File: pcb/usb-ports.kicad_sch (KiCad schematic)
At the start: 10 parts, among them J6 USB4105-GF-A, J7 USB4105-GF-A, U2 USBLC6-2P6, U3 USBLC6-2P6

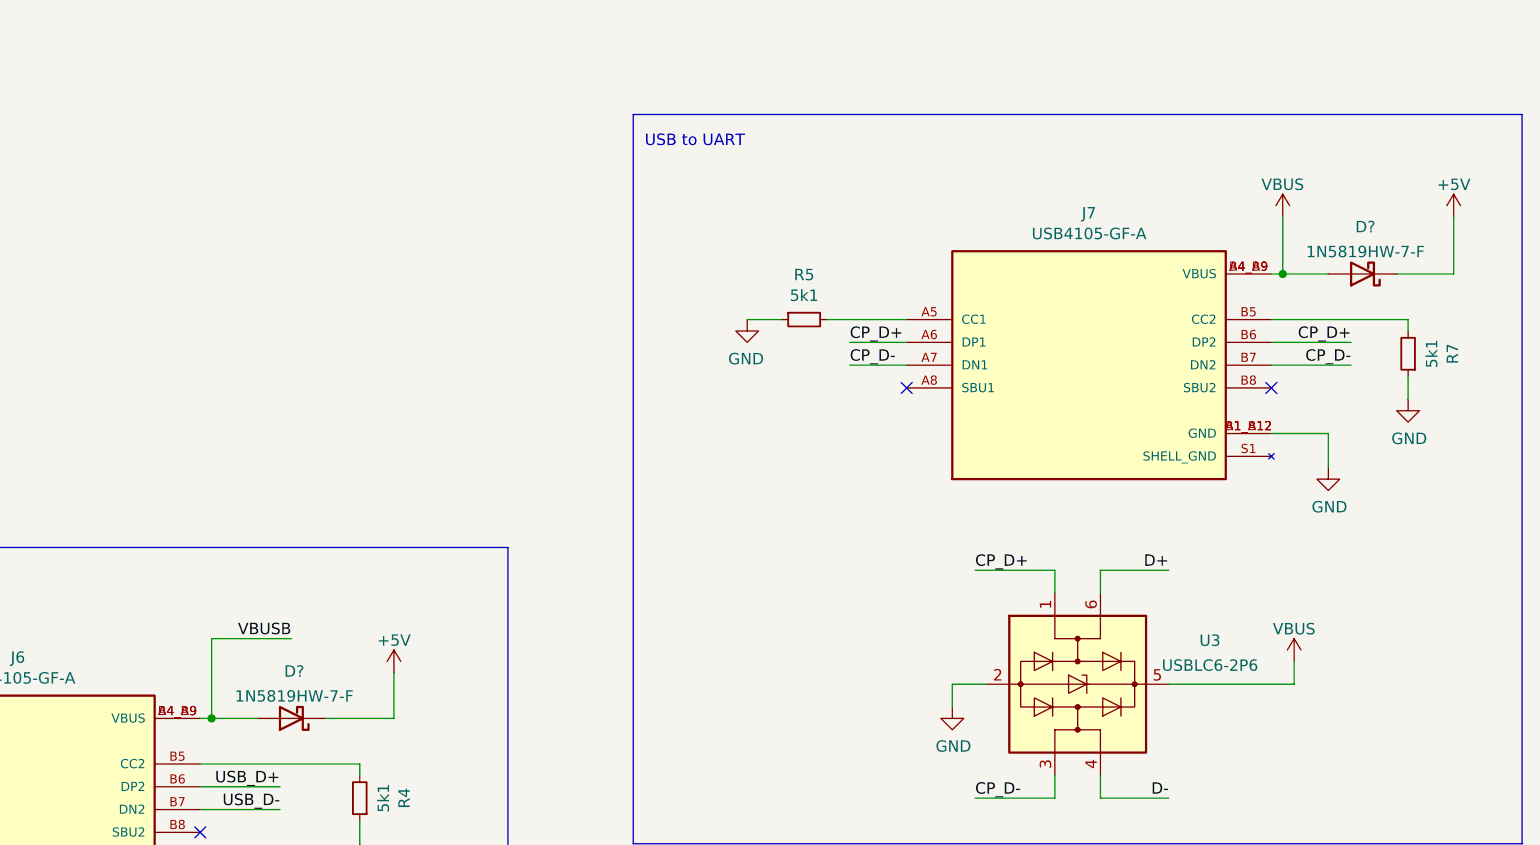
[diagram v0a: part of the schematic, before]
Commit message: Added first version of the pcb layout
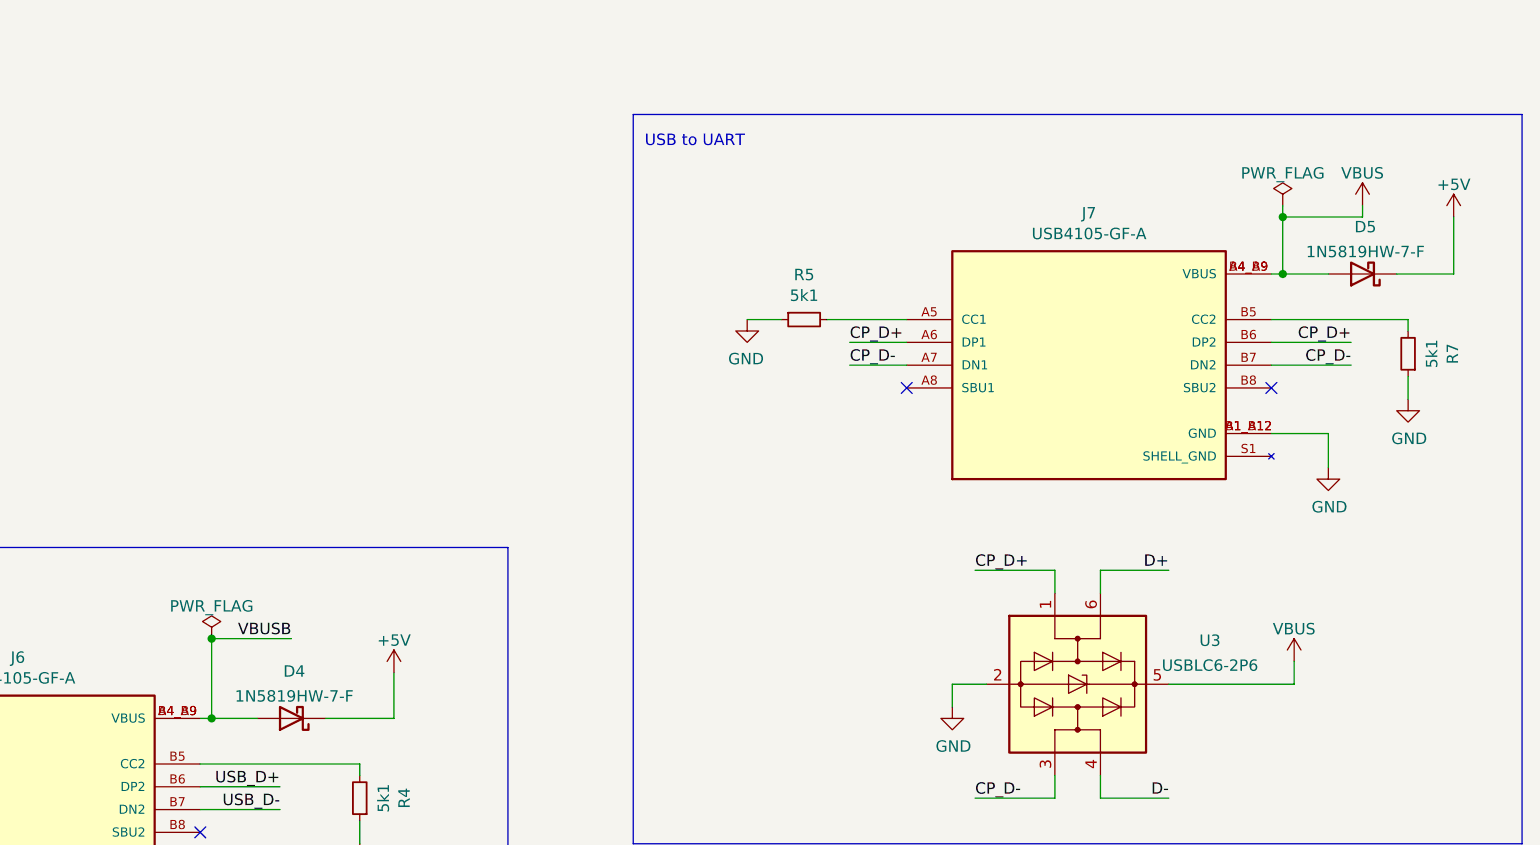
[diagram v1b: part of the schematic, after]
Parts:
- D4, D5: renamed from D?; footprint Diode_THT:D_DO-41_SOD81_P10.16mm_Horizontal -> Diode_SMD:D_SOD-123
- J6, J7: footprint GCT_USB4105-GF-A -> USB4105-GF-A:GCT_USB4105-GF-A
